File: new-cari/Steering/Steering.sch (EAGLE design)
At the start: 46 parts, among them J1 UX60-MB-5S8, J2 AVR_SPI_PROG_3X2TESTPOINTS, J3 MOLEX_5025850670, J4 NONASSMANN_VGA_CONNECTOR, J5 PCB_SCREW_TERM_8, J6 PCB_SCREW_TERM_6, J7 PCB_SCREW_TERM_3, J8 B2PS-VH(LF)(SN), U1 CD4066BPWR, U2 CD4066BPWR, X1 TSX-3225 16.0000MF18X-AC0

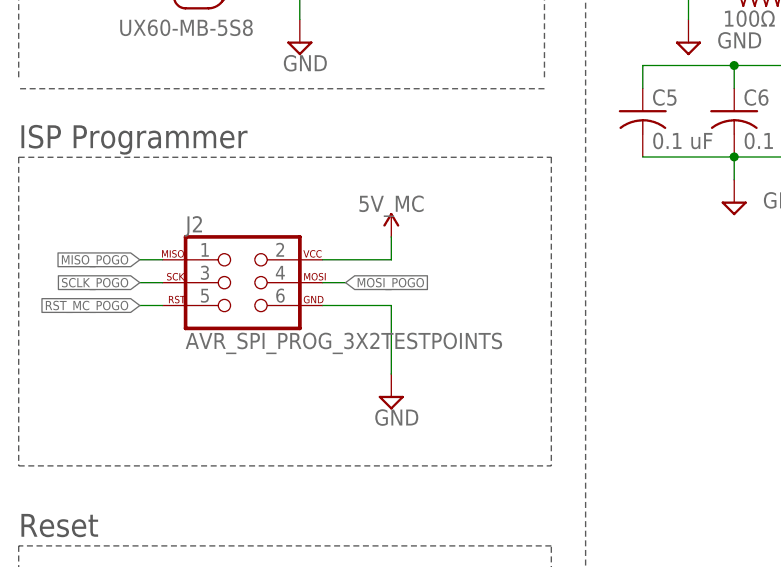
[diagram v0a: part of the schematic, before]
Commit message: Replaced Pogo Header
Switched out the pogo header for a properly sized (larger) one.
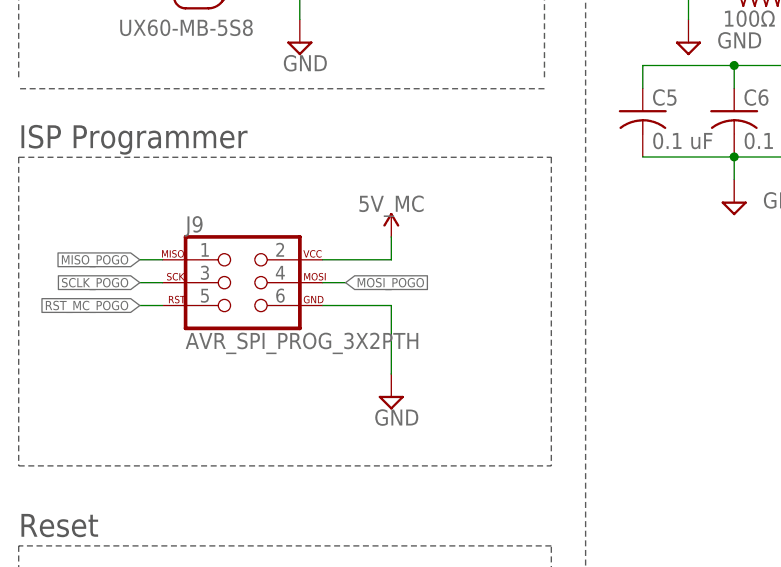
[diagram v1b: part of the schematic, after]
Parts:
- removed J2: AVR_SPI_PROG_3X2TESTPOINTS, SparkFun-Connectors:AVR_SPI_PROG_3X2TESTPOINTS
- added J9: AVR_SPI_PROG_3X2PTH, SparkFun-Connectors:AVR_SPI_PROG_3X2PTH
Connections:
- net 5V_MC: now also J9.2; no longer J2.2
- net GND: now also J9.6; no longer J2.6
- net MISO_POGO: now also J9.1; no longer J2.1
- net MOSI_POGO: now also J9.4; no longer J2.4
- net RST_MC_POGO: now also J9.5; no longer J2.5
- net SCLK_POGO: now also J9.3; no longer J2.3
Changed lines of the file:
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@@
 <part name="J1" library="RoboJackets-Connectors" deviceset="UX60*-MB-5S?" device="8"/>
 <part name="C11" library="resistor" library_urn="urn:adsk.eagle:library:348" deviceset="C-US" device="C0603" package3d_urn="urn:adsk.eagle:package:26138/1" value="0.1 uF"/>
-<part name="J2" library="SparkFun-Connectors" library_urn="urn:adsk.eagle:library:513" deviceset="AVR_SPI_PROG_3X2" device="TESTPOINTS" package3d_urn="urn:adsk.eagle:package:38008/1" value="AVR_SPI_PROG_3X2TESTPOINTS"/>
 <part name="SUPPLY14" library="supply2" library_urn="urn:adsk.eagle:library:372" deviceset="GND" device=""/>
 <part name="SUPPLY22" library="SparkFun-PowerSymbols" library_urn="urn:adsk.eagle:library:530" deviceset="VCC_2" device="" value="5V_MC"/>
@@
 <part name="TP2" library="SparkFun-Connectors" library_urn="urn:adsk.eagle:library:513" deviceset="TEST-POINT" device="TP_15TH_THRU" package3d_urn="urn:adsk.eagle:package:38288/1"/>
 <part name="SUPPLY15" library="supply2" library_urn="urn:adsk.eagle:library:372" deviceset="GND" device=""/>
+<part name="J9" library="SparkFun-Connectors" library_urn="urn:adsk.eagle:library:513" deviceset="AVR_SPI_PROG_3X2" device="PTH" package3d_urn="urn:adsk.eagle:package:38016/1"/>
 </parts>
 <sheets>
@@
 <attribute name="VALUE" x="39.751" y="173.736" size="1.778" layer="96" rot="R90"/>
 </instance>
-<instance part="J2" gate="G$1" x="33.02" y="214.63" smashed="yes">
-<attribute name="NAME" x="27.94" y="220.218" size="1.778" layer="95" font="vector"/>
-<attribute name="VALUE" x="27.94" y="207.264" size="1.778" layer="96" font="vector"/>
-</instance>
 <instance part="SUPPLY14" gate="GND" x="50.8" y="201.93" smashed="yes">
 <attribute name="VALUE" x="48.895" y="198.755" size="1.778" layer="96"/>
@@
 <instance part="SUPPLY15" gate="GND" x="88.9" y="223.52" smashed="yes">
 <attribute name="VALUE" x="92.075" y="222.885" size="1.778" layer="96"/>
+</instance>
+<instance part="J9" gate="G$1" x="33.02" y="214.63" smashed="yes">
+<attribute name="NAME" x="27.94" y="220.218" size="1.778" layer="95" font="vector"/>
+<attribute name="VALUE" x="27.94" y="207.264" size="1.778" layer="96" font="vector"/>
 </instance>
 </instances>
@@
 </segment>
 <segment>
-<pinref part="J2" gate="G$1" pin="6"/>
 <wire x1="43.18" y1="212.09" x2="50.8" y2="212.09" width="0.1524" layer="91"/>
 <pinref part="SUPPLY14" gate="GND" pin="GND"/>
 <wire x1="50.8" y1="212.09" x2="50.8" y2="204.47" width="0.1524" layer="91"/>
+<pinref part="J9" gate="G$1" pin="6"/>
 </segment>
 <segment>
@@
 <segment>
 <pinref part="SUPPLY22" gate="G$1" pin="VCC_2"/>
-<pinref part="J2" gate="G$1" pin="2"/>
 <wire x1="50.8" y1="219.71" x2="50.8" y2="217.17" width="0.1524" layer="91"/>
 <wire x1="50.8" y1="217.17" x2="43.18" y2="217.17" width="0.1524" layer="91"/>
+<pinref part="J9" gate="G$1" pin="2"/>
 </segment>
 <segment>
@@
 </segment>
 <segment>
-<pinref part="J2" gate="G$1" pin="3"/>
 <wire x1="25.4" y1="214.63" x2="22.86" y2="214.63" width="0.1524" layer="91"/>
 <label x="22.86" y="214.63" size="1.016" layer="95" rot="R180" xref="yes"/>
+<pinref part="J9" gate="G$1" pin="3"/>
 </segment>
 </net>
@@
 </segment>
 <segment>
-<pinref part="J2" gate="G$1" pin="4"/>
 <wire x1="43.18" y1="214.63" x2="45.72" y2="214.63" width="0.1524" layer="91"/>
 <label x="45.72" y="214.63" size="1.016" layer="95" xref="yes"/>
+<pinref part="J9" gate="G$1" pin="4"/>
 </segment>
 </net>
@@
 </segment>
 <segment>
-<pinref part="J2" gate="G$1" pin="1"/>
 <wire x1="25.4" y1="217.17" x2="22.86" y2="217.17" width="0.1524" layer="91"/>
 <label x="22.86" y="217.17" size="1.016" layer="95" rot="R180" xref="yes"/>
+<pinref part="J9" gate="G$1" pin="1"/>
 </segment>
 </net>
@@
 </segment>
 <segment>
-<pinref part="J2" gate="G$1" pin="5"/>
 <wire x1="25.4" y1="212.09" x2="22.86" y2="212.09" width="0.1524" layer="91"/>
 <label x="22.86" y="212.09" size="1.016" layer="95" rot="R180" xref="yes"/>
-</segment>
-</net>
+<pinref part="J9" gate="G$1" pin="5"/>
+</segment>
+</net>

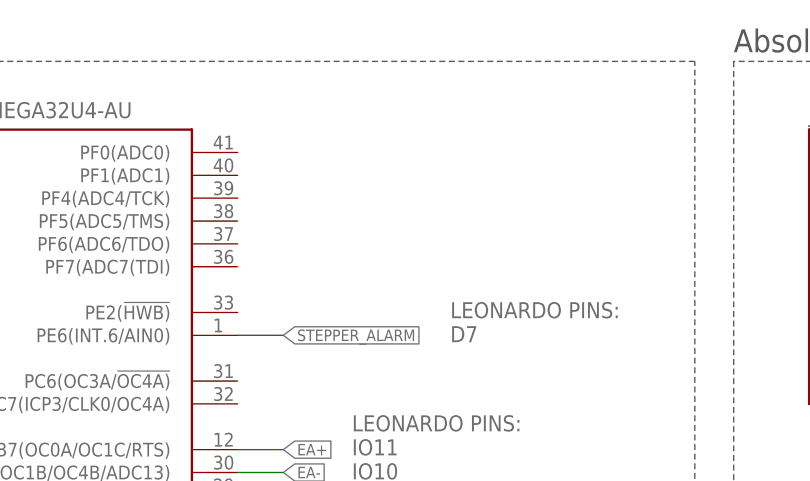
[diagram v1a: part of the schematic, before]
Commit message: Added Status LED
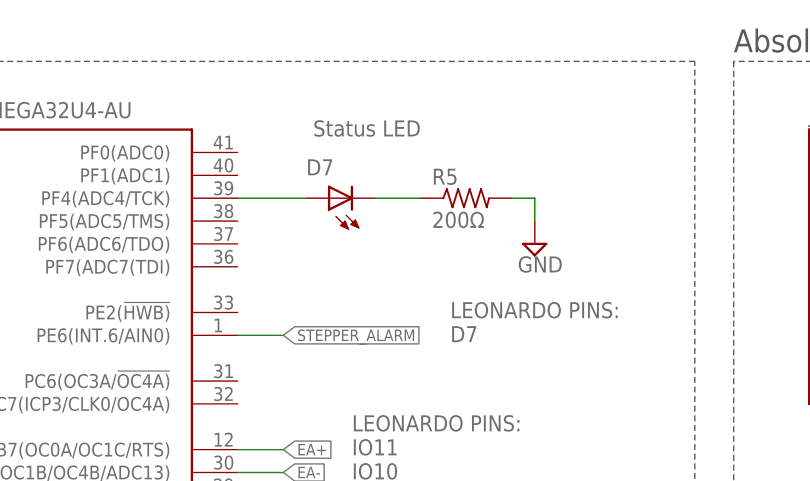
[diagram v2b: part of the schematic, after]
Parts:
- added D7: BLUE, RoboJackets-LEDs:LED-SMD-BLUE
- added R5: 200Ω, RoboJackets-Resistors:R0603W
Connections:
- new net N$2: D7.A, MC1.PF4(ADC4/TCK)
- new net N$3: D7.K, R5.PIN1
- net GND: now also R5.PIN2
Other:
- note added: "Status LED"
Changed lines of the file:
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@@
 <part name="SUPPLY15" library="supply2" library_urn="urn:adsk.eagle:library:372" deviceset="GND" device=""/>
 <part name="J9" library="SparkFun-Connectors" library_urn="urn:adsk.eagle:library:513" deviceset="AVR_SPI_PROG_3X2" device="PTH" package3d_urn="urn:adsk.eagle:package:38016/1"/>
+<part name="D7" library="RoboJackets-LEDs" deviceset="LED-SMD" device="" technology="-BLUE" value="BLUE"/>
+<part name="R5" library="RoboJackets-Resistors" deviceset="R0603W" device="" value="200Ω"/>
+<part name="SUPPLY16" library="supply2" library_urn="urn:adsk.eagle:library:372" deviceset="GND" device=""/>
 </parts>
 <sheets>
@@
 <text x="105.918" y="138.136" size="2.54" layer="97">SPI Select Switches</text>
 <text x="380.238" y="77.724" size="1.778" layer="97">Screw Terminal to Stepper</text>
+<text x="183.642" y="260.858" size="1.778" layer="95">Status LED</text>
 </plain>
 <instances>
@@
 <attribute name="NAME" x="27.94" y="220.218" size="1.778" layer="95" font="vector"/>
 <attribute name="VALUE" x="27.94" y="207.264" size="1.778" layer="96" font="vector"/>
+</instance>
+<instance part="D7" gate="G$1" x="187.96" y="254" smashed="yes" rot="R90">
+<attribute name="NAME" x="182.88" y="256.54" size="1.778" layer="95"/>
+</instance>
+<instance part="R5" gate="G$1" x="200.66" y="254" smashed="yes">
+<attribute name="NAME" x="196.85" y="255.4986" size="1.778" layer="95"/>
+<attribute name="VALUE" x="196.85" y="250.698" size="1.778" layer="96"/>
+</instance>
+<instance part="SUPPLY16" gate="GND" x="208.28" y="248.92" smashed="yes">
+<attribute name="VALUE" x="206.375" y="245.745" size="1.778" layer="96"/>
 </instance>
 </instances>
@@
 <wire x1="88.9" y1="228.6" x2="78.74" y2="228.6" width="0.1524" layer="91"/>
 <wire x1="88.9" y1="228.6" x2="88.9" y2="226.06" width="0.1524" layer="91"/>
+</segment>
+<segment>
+<pinref part="R5" gate="G$1" pin="PIN2"/>
+<wire x1="205.74" y1="254" x2="208.28" y2="254" width="0.1524" layer="91"/>
+<wire x1="208.28" y1="254" x2="208.28" y2="251.46" width="0.1524" layer="91"/>
+<pinref part="SUPPLY16" gate="GND" pin="GND"/>
 </segment>
 </net>
@@
 </segment>
 </net>
+<net name="N$2" class="0">
+<segment>
+<pinref part="MC1" gate="G$1" pin="PF4(ADC4/TCK)"/>
+<wire x1="175.26" y1="254" x2="182.88" y2="254" width="0.1524" layer="91"/>
+<pinref part="D7" gate="G$1" pin="A"/>
+</segment>
+</net>
+<net name="N$3" class="0">
+<segment>
+<pinref part="R5" gate="G$1" pin="PIN1"/>
+<pinref part="D7" gate="G$1" pin="K"/>
+<wire x1="195.58" y1="254" x2="190.5" y2="254" width="0.1524" layer="91"/>
+</segment>
+</net>

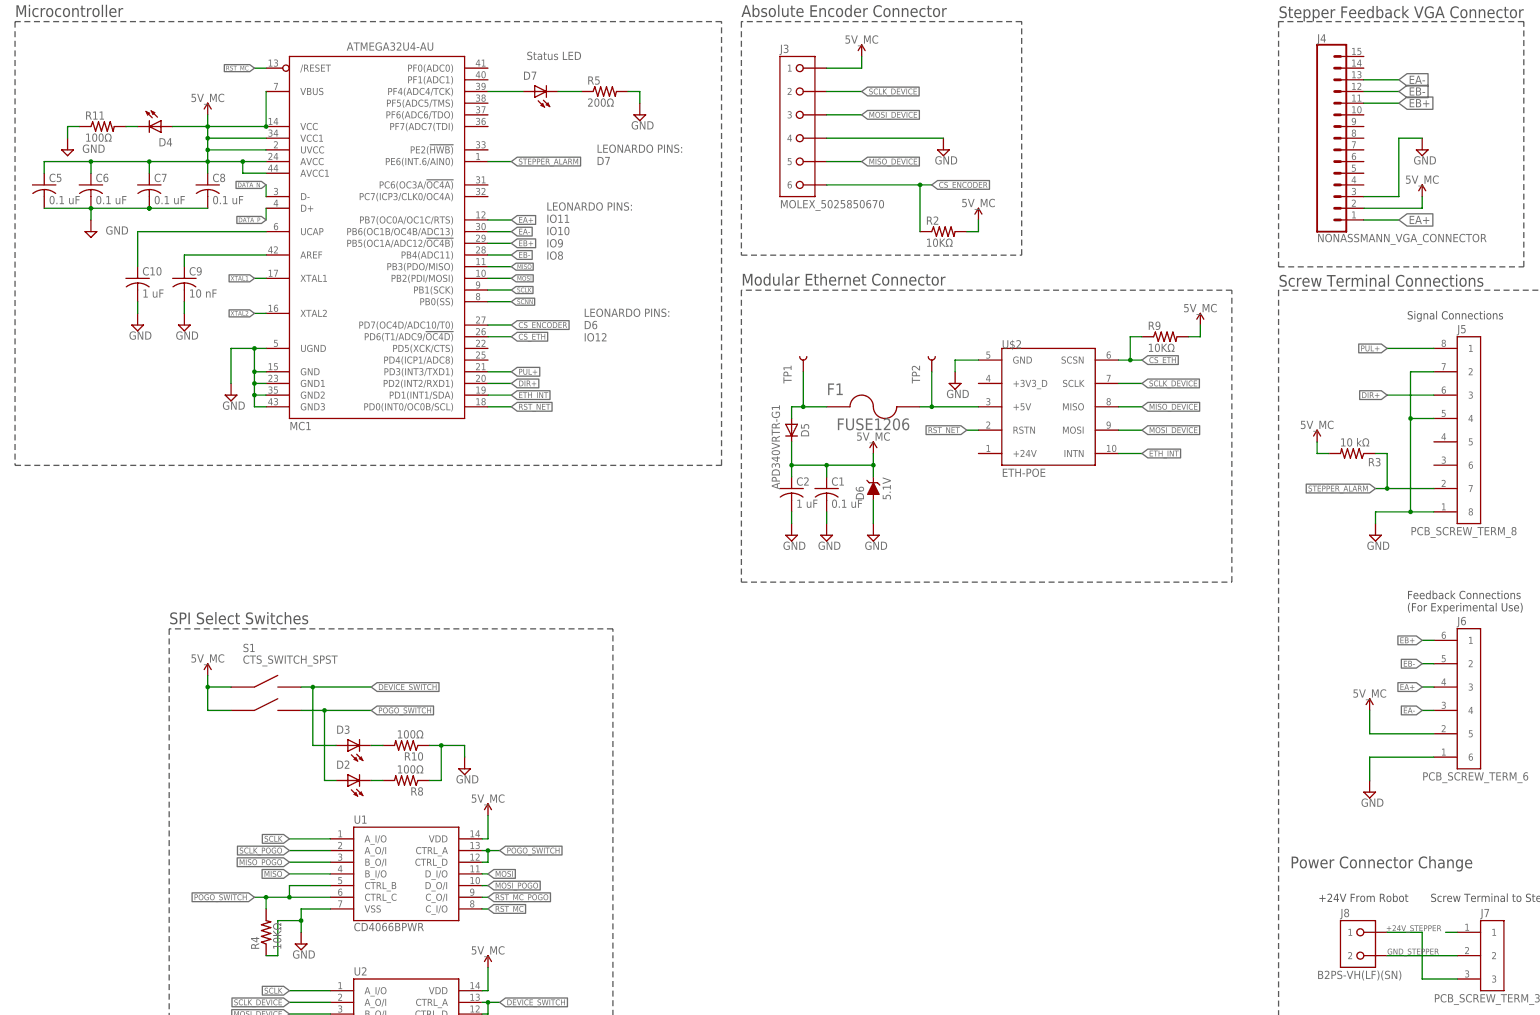
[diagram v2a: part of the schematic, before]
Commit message: Added indicator LED
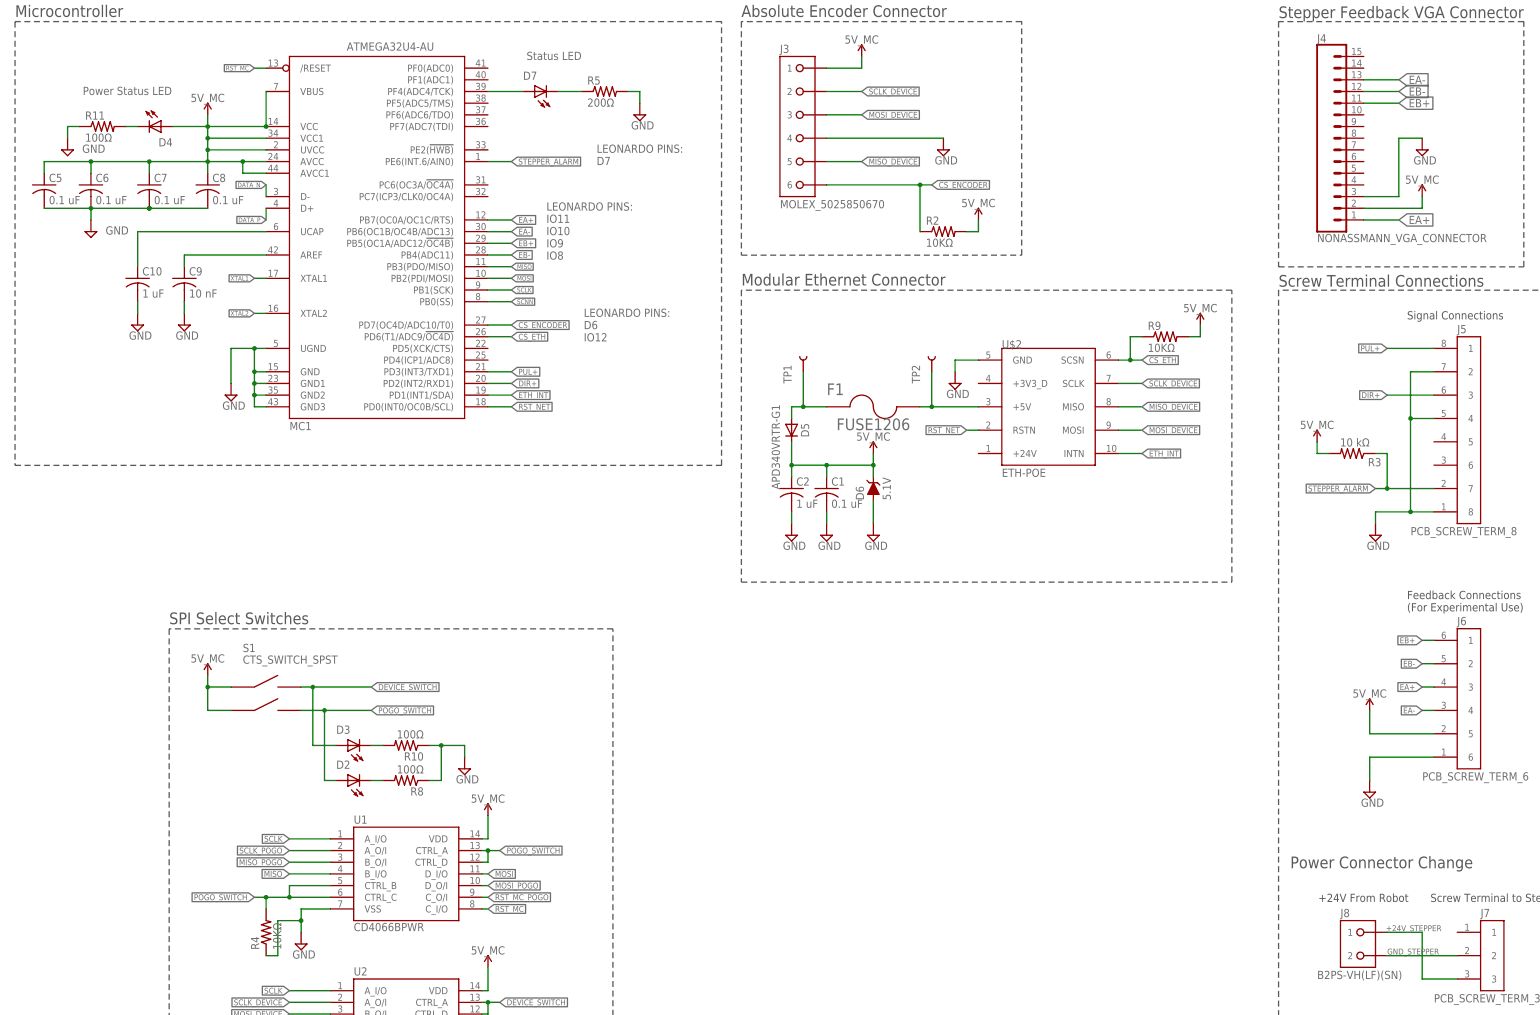
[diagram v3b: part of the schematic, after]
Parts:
- D4: value LED_AA3528VRVCS/A -> PINK
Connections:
- removed net N$7: J7.1
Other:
- note added: "Power Status LED"
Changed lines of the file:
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@@
 <part name="D2" library="Steering" deviceset="LED_AA3528VRVCS/A" device=""/>
 <part name="R8" library="RoboJackets-Resistors" deviceset="R0603W" device="" value="100Ω"/>
-<part name="D4" library="Steering" deviceset="LED_AA3528VRVCS/A" device=""/>
+<part name="D4" library="Steering" deviceset="LED_AA3528VRVCS/A" device="" value="PINK"/>
 <part name="R11" library="RoboJackets-Resistors" deviceset="R0603W" device="" value="100Ω"/>
 <part name="SUPPLY30" library="supply2" library_urn="urn:adsk.eagle:library:372" deviceset="GND" device=""/>
@@
 <text x="380.238" y="77.724" size="1.778" layer="97">Screw Terminal to Stepper</text>
 <text x="183.642" y="260.858" size="1.778" layer="95">Status LED</text>
+<text x="87.122" y="253.238" size="1.778" layer="95">Power Status LED</text>
 </plain>
 <instances>
@@
 </segment>
 </net>
-<net name="N$7" class="0">
-<segment>
-<pinref part="J7" gate="G$1" pin="1"/>
-<wire x1="386.08" y1="71.12" x2="383.54" y2="71.12" width="0.1524" layer="91"/>
-</segment>
-</net>

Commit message: Board and CAD Updates
-Made changes recommended in informal design review
-Exported Board file to Inventor and continued CAD assembly
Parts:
- added C12, C13: 0.1 uF, resistor:C-USC0603
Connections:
- net 5V_MC: now also C12.1, C13.1
- net GND: now also C12.2, C13.2, U2.C_I/O, U2.C_O/I
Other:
- moved on the sheet: D4, R11
